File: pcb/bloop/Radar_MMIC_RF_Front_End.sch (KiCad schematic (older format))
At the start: 3 parts

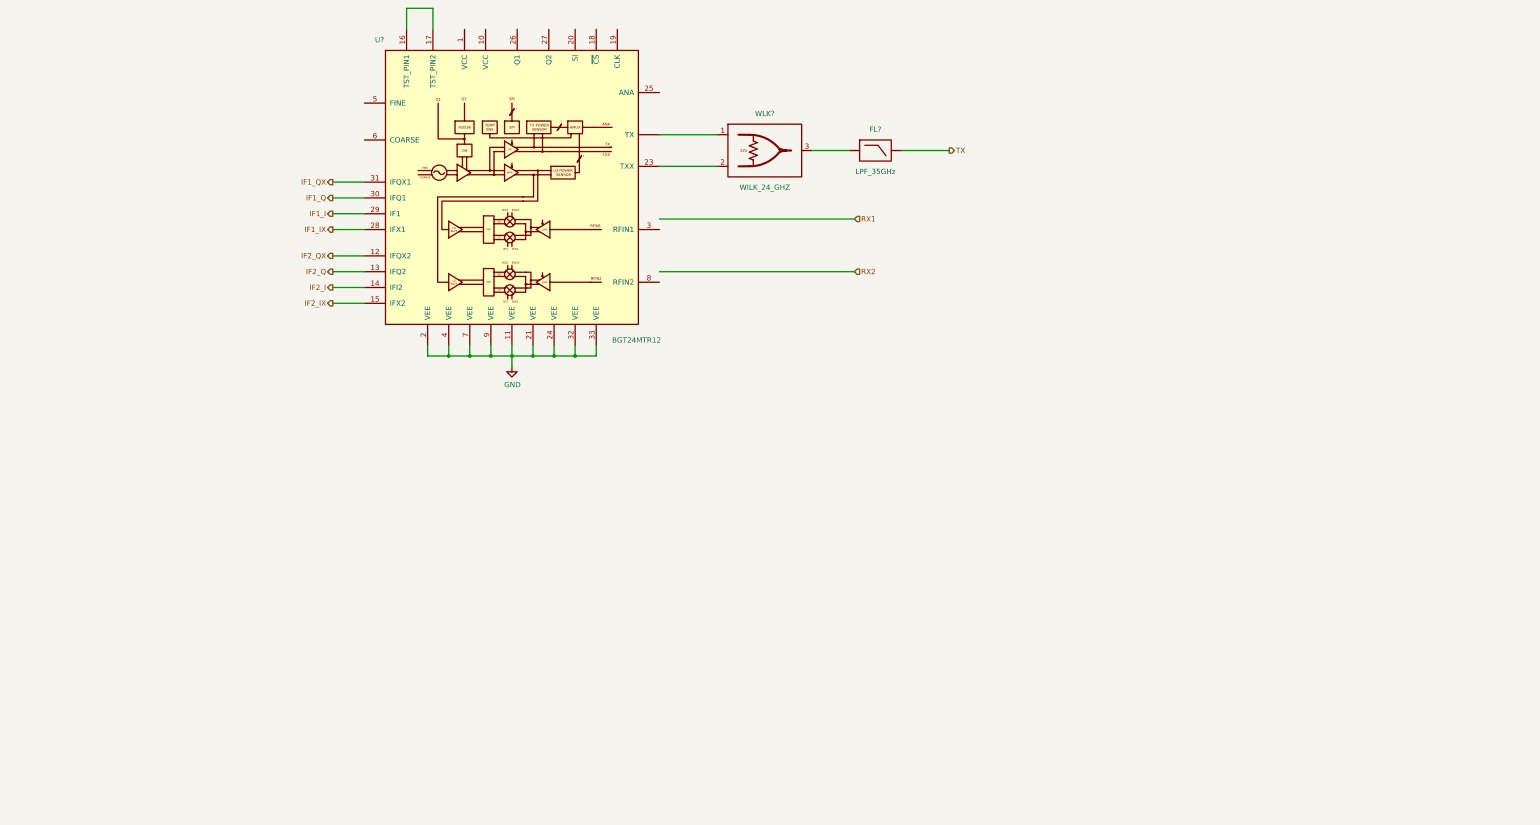
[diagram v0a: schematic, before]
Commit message: Started PLL circuitry Added PLL device and oscillator Still need loop filter and clock filter circuits
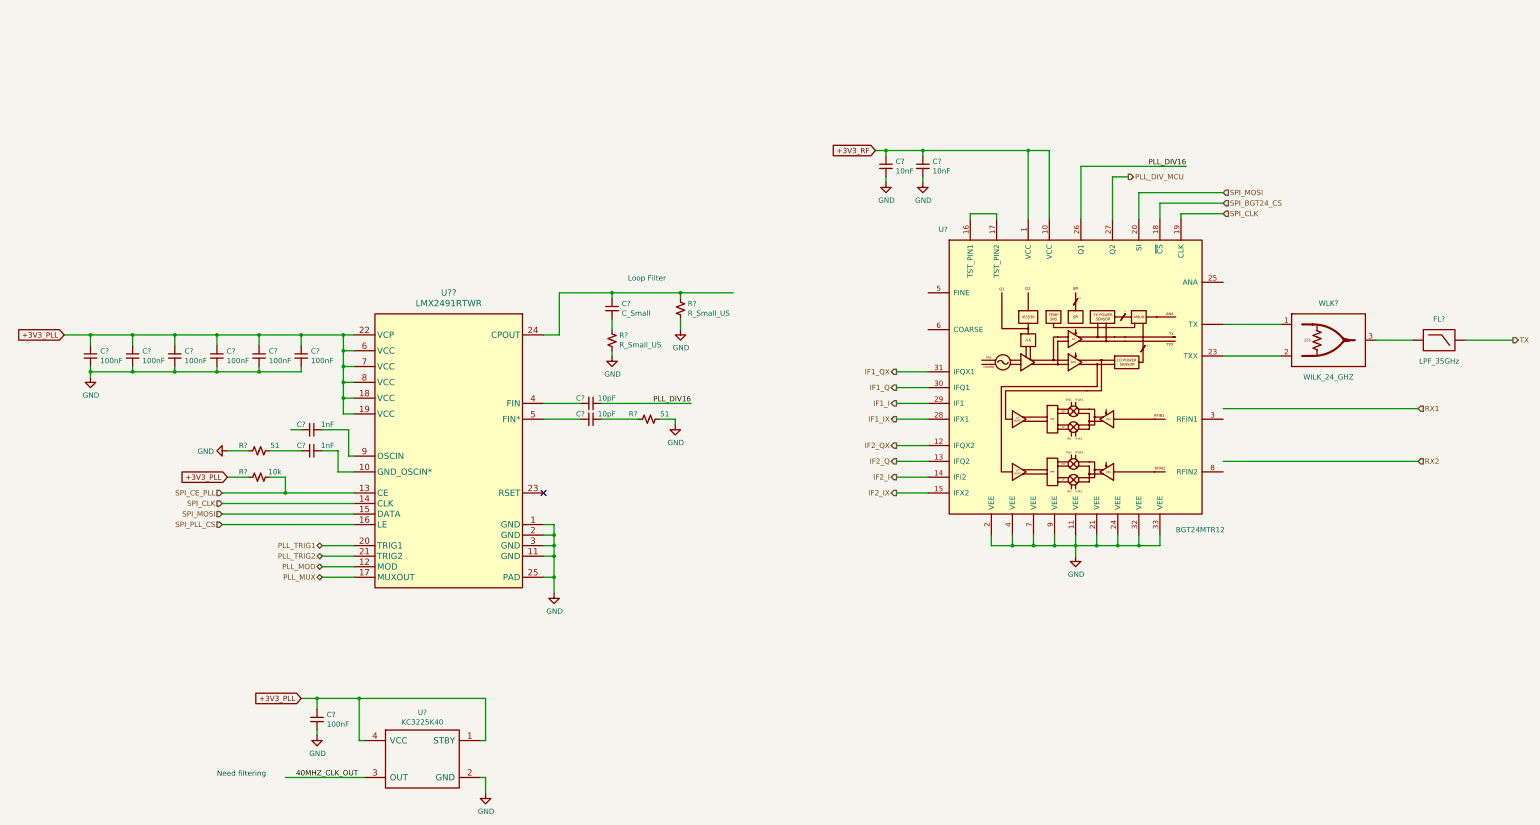
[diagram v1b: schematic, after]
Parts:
- added C? (x2): 10pF, symbol Device:C_Small
- added C? (x2): 10nF, symbol Device:C_Small
- added C? (x7): 100nF, symbol Device:C_Small
- added C? (x2): 1nF, symbol Device:C_Small
- added C?: C_Small, symbol Device:C_Small
- added R? (x2): 51, symbol Device:R_Small_US
- added R?: 10k, symbol Device:R_Small_US
- added R? (x2): R_Small_US, symbol Device:R_Small_US
- added U?: KC3225K40, Crystal:Crystal_SMD_3225-4Pin_3.2x2.5mm, symbol bloop:KC3225K40
- added U??: LMX2491RTWR, Package_DFN_QFN:VQFN-24-1EP_4x4mm_P0.5mm_EP2.45x2.45mm, symbol bloop:LMX2491RTWR
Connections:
- net labels added: +3V3_PLL, +3V3_RF, 40MHZ_CLK_OUT, PLL_DIV16, PLL_DIV_MCU, PLL_MOD, PLL_MUX, PLL_TRIG1, PLL_TRIG2, SPI_BGT24_CS, SPI_CE_PLL, SPI_CLK, SPI_MOSI, SPI_PLL_CS
- wire segments 35 -> 150
- no-connect marks 0 -> 1
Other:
- note added: "Loop Filter"
- note added: "Need filtering"
- moved on the sheet: FL?, U?, WLK?

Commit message: Add DC blocking capacitors; add larger resistor and capacitor symbols; implement root PN for symbols
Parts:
- removed C? (x2): 10pF, symbol Device:C_Small
- removed C? (x2): 10nF, symbol Device:C_Small
- removed C? (x7): 100nF, symbol Device:C_Small
- removed C? (x2): 1nF, symbol Device:C_Small
- removed C?: C_Small, symbol Device:C_Small
- removed R? (x2): 51, symbol Device:R_Small_US
- removed R?: 10k, symbol Device:R_Small_US
- removed R? (x2): R_Small_US, symbol Device:R_Small_US
- added C? (x7): 100n, symbol Device:C
- added C?: C, symbol Device:C
- added C? (x2): 10p, symbol Device:C
- added C? (x2): 1n, symbol Device:C
- added C? (x2): 10n, symbol Device:C
- added R? (x2): R_US, symbol Device:R_US
- added R? (x2): 51, symbol Device:R_US
- added R?: 10k, symbol Device:R_US
- U?: renamed from U??; value LMX2491RTWR -> LMX2491; symbol bloop:LMX2491RTWR -> bloop:LMX2491; Manufacturer PN (none) -> LMX2491RTWR
- U?: value KC3225K40 -> KC3225K; symbol bloop:KC3225K40 -> bloop:KC3225K; Manufacturer PN (none) -> KC3225K40
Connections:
- wire segments 150 -> 156
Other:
- note added: "Crystal oscillator"
- moved on the sheet: FL?, U?, WLK?

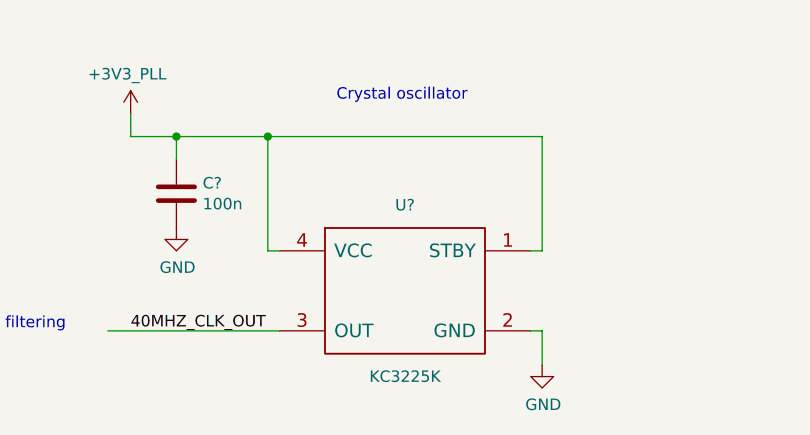
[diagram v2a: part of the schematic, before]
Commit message: fixing MPNs
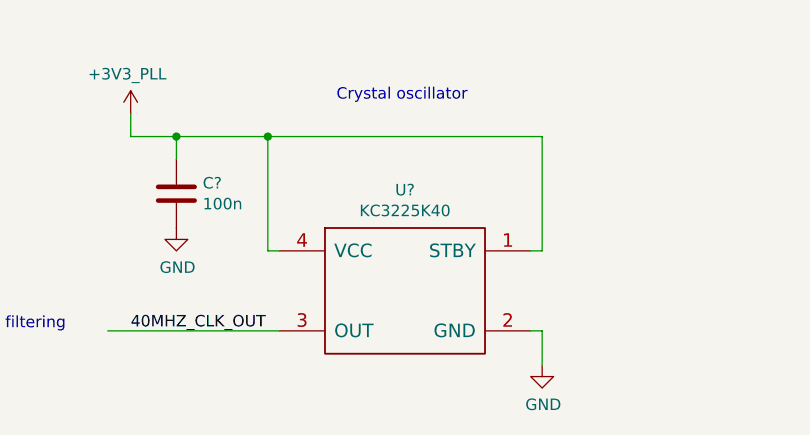
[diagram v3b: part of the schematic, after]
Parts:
- removed U?: KC3225K, Crystal:Crystal_SMD_3225-4Pin_3.2x2.5mm, symbol bloop:KC3225K
- added U?: KC3225K40, Crystal:Crystal_SMD_3225-4Pin_3.2x2.5mm, symbol bloop:KC3225K40
- U?: MPN (none) -> LMX2491RTWR; Manufacturer PN LMX2491RTWR -> (none)
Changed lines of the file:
@@
 	4200 6250 3400 6250
-$Comp
-L bloop:KC3225K U?
-U 1 1 5D6FD5C8
-P 5100 8100
-F 0 "U?" H 5100 8500 50  0000 C CNN
-F 1 "KC3225K" H 5100 7750 50  0000 C CNN
-F 2 "Crystal:Crystal_SMD_3225-4Pin_3.2x2.5mm" H 5100 8100 50  0001 C CNN
-F 3 "https://global.kyocera.com/prdct/electro/product/pdf/clock_k_e.pdf" H 5100 8100 50  0001 C CNN
-F 4 "KC3225K40" H 5100 8100 50  0001 C CNN "Manufacturer PN"
-	1    5100 8100
-	1    0    0    -1
-$EndComp
 $Comp
 L bloop:LMX2491 U?
@@
 F 2 "Package_DFN_QFN:VQFN-24-1EP_4x4mm_P0.5mm_EP2.45x2.45mm" H 5100 5050 60  0001 C CNN
 F 3 "http://www.ti.com/lit/ds/symlink/lmx2491.pdf" H 5100 5250 60  0001 C CNN
-F 4 "LMX2491RTWR" H 5100 5250 50  0001 C CNN "Manufacturer PN"
+F 4 "LMX2491RTWR" H 5100 5250 50  0001 C CNN "MPN"
 	1    5100 5250
 	1    0    0    -1
@@
 	12100 2800 13100 2800
 Connection ~ 11600 2800
+$Comp
+L bloop:KC3225K40 U?
+U 1 1 5D4329C9
+P 5100 8100
+F 0 "U?" H 5100 8566 50  0000 C CNN
+F 1 "KC3225K40" H 5100 8475 50  0000 C CNN
+F 2 "Crystal:Crystal_SMD_3225-4Pin_3.2x2.5mm" H 5100 8100 50  0001 C CNN
+F 3 "https://global.kyocera.com/prdct/electro/product/pdf/clock_k_e.pdf" H 5100 8100 50  0001 C CNN
+F 4 "KC3225K40.0000C1GE00" H 5100 8100 50  0001 C CNN "MPN"
+	1    5100 8100
+	1    0    0    -1
+$EndComp
 $EndSCHEMATC

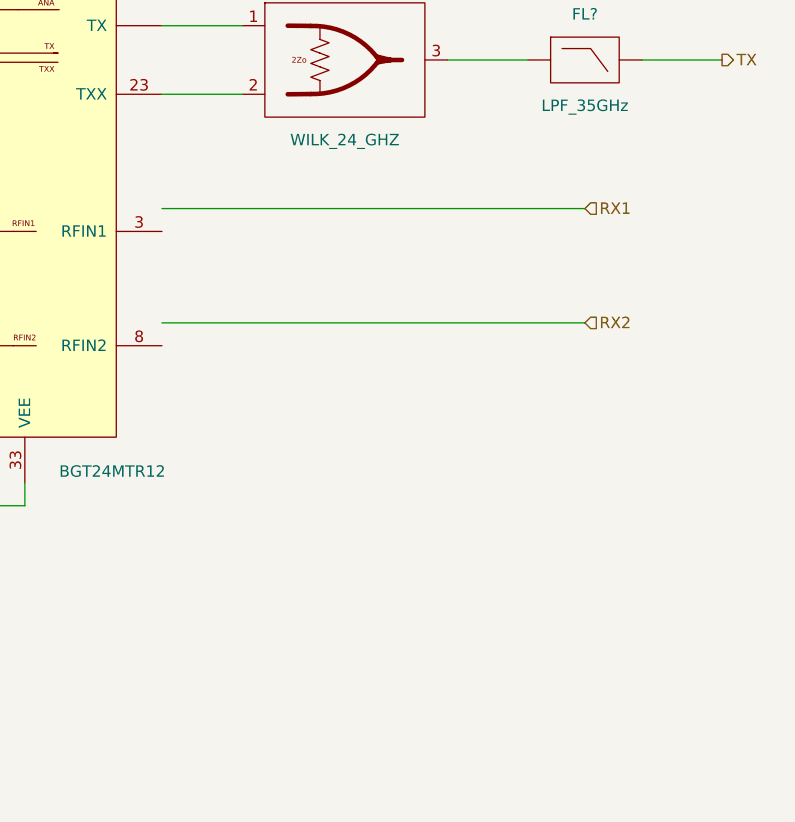
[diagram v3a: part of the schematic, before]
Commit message: Add stubs to RX portion; move blocking caps
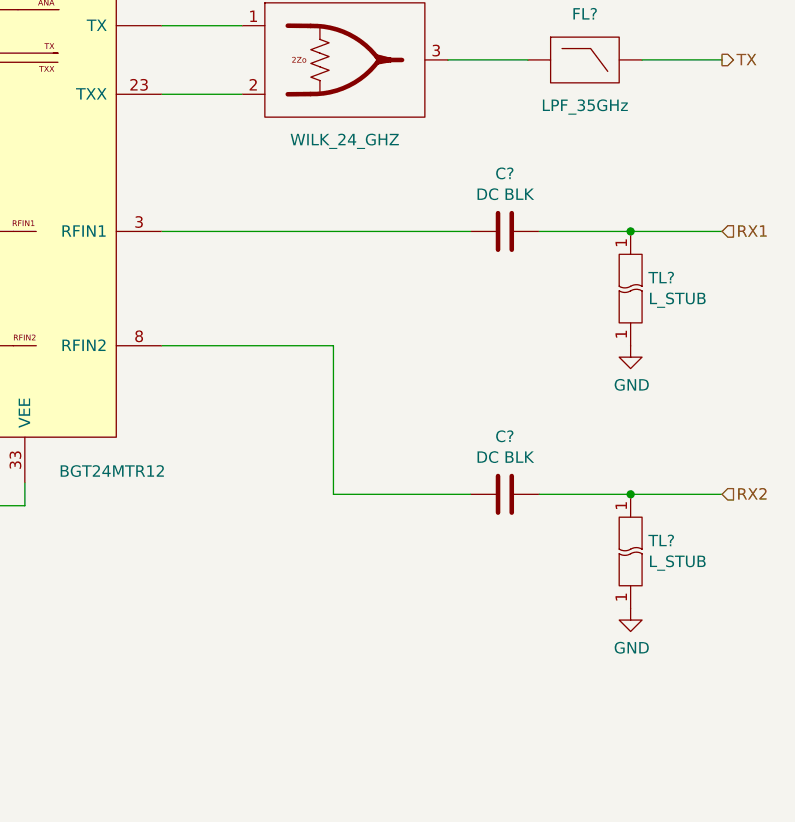
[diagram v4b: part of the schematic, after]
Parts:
- added C? (x2): DC BLK, symbol Device:C
- added TL? (x2): L_STUB, symbol bloop:L_STUB
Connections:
- wire segments 156 -> 162
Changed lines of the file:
@@
 EESchema Schematic File Version 4
 LIBS:bloop-cache
-EELAYER 29 0
+EELAYER 30 0
 EELAYER END
 $Descr B 17000 11000
@@
 	1    0    0    -1
 $EndComp
-Text HLabel 15900 4650 2    50   Output ~ 0
-TX
-Text HLabel 15300 5300 2    50   Input ~ 0
+Text HLabel 15900 5400 2    50   Input ~ 0
 RX1
-Text HLabel 15300 5800 2    50   Input ~ 0
+Text HLabel 15900 6550 2    50   Input ~ 0
 RX2
 $Comp
@@
 Wire Wire Line
 	12050 6700 12050 6600
-Wire Wire Line
-	15300 5300 13450 5300
-Wire Wire Line
-	13450 5800 15300 5800
 $Comp
 L bloop:WILK_24_GHZ WLK?
@@
 	1    0    0    -1
 $EndComp
+$Comp
+L Device:C C?
+U 1 1 5D4BA537
+P 14950 5400
+AR Path="/5D3D1628/5D4BA537" Ref="C?"  Part="1"
+AR Path="/5D4BA537" Ref="C?"  Part="1"
+F 0 "C?" V 14698 5400 50  0000 C CNN
+F 1 "DC BLK" V 14789 5400 50  0000 C CNN
+F 2 "" H 14988 5250 50  0001 C CNN
+F 3 "~" H 14950 5400 50  0001 C CNN
+	1    14950 5400
+	0    1    1    0
+$EndComp
+$Comp
+L power:GND #PWR?
+U 1 1 5D4EBBB7
+P 15500 5900
+F 0 "#PWR?" H 15500 5650 50  0001 C CNN
+F 1 "GND" H 15505 5727 50  0000 C CNN
+F 2 "" H 15500 5900 50  0001 C CNN
+F 3 "" H 15500 5900 50  0001 C CNN
+	1    15500 5900
+	1    0    0    -1
+$EndComp
+Text HLabel 15900 4650 2    50   Output ~ 0
+TX
+Wire Wire Line
+	14800 5400 13450 5400
+$Comp
+L Device:C C?
+U 1 1 5D5604D1
+P 14950 6550
+AR Path="/5D3D1628/5D5604D1" Ref="C?"  Part="1"
+AR Path="/5D5604D1" Ref="C?"  Part="1"
+F 0 "C?" V 14698 6550 50  0000 C CNN
+F 1 "DC BLK" V 14789 6550 50  0000 C CNN
+F 2 "" H 14988 6400 50  0001 C CNN
+F 3 "~" H 14950 6550 50  0001 C CNN
+	1    14950 6550
+	0    1    1    0
+$EndComp
+$Comp
+L power:GND #PWR?
+U 1 1 5D5604DF
+P 15500 7050
+F 0 "#PWR?" H 15500 6800 50  0001 C CNN
+F 1 "GND" H 15505 6877 50  0000 C CNN
+F 2 "" H 15500 7050 50  0001 C CNN
+F 3 "" H 15500 7050 50  0001 C CNN
+	1    15500 7050
+	1    0    0    -1
+$EndComp
+Wire Wire Line
+	14800 6550 14200 6550
+Wire Wire Line
+	14200 6550 14200 5900
+Wire Wire Line
+	14200 5900 13450 5900
+$Comp
+L bloop:L_STUB TL?
+U 1 1 5D5A19BF
+P 15500 5650
+F 0 "TL?" V 15546 5572 50  0000 R CNN
+F 1 "L_STUB" V 15455 5572 50  0000 R CNN
+F 2 "" H 15500 5800 50  0001 C CNN
+F 3 "" H 15500 5800 50  0001 C CNN
+F 4 "N/A" H 15500 5650 50  0001 C CNN "MPN"
+F 5 "97.24 mils" H 15500 5400 50  0001 C CNN "Length"
+F 6 "7.87 mils" H 15500 5300 50  0001 C CNN "Width"
+	1    15500 5650
+	0    -1   -1   0
+$EndComp
+Wire Wire Line
+	15100 5400 15500 5400
+Connection ~ 15500 5400
+Wire Wire Line
+	15500 5400 15900 5400
+Wire Wire Line
+	15100 6550 15500 6550
+$Comp
+L bloop:L_STUB TL?
+U 1 1 5D5C0F4D
+P 15500 6800
+F 0 "TL?" V 15546 6722 50  0000 R CNN
+F 1 "L_STUB" V 15455 6722 50  0000 R CNN
+F 2 "" H 15500 6950 50  0001 C CNN
+F 3 "" H 15500 6950 50  0001 C CNN
+F 4 "N/A" H 15500 6800 50  0001 C CNN "MPN"
+F 5 "97.24 mils" H 15500 6550 50  0001 C CNN "Length"
+F 6 "7.87 mils" H 15500 6450 50  0001 C CNN "Width"
+	1    15500 6800
+	0    -1   -1   0
+$EndComp
+Connection ~ 15500 6550
+Wire Wire Line
+	15500 6550 15900 6550
 $EndSCHEMATC
